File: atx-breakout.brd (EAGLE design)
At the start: 160 x 100 mm, 103 parts, among them J1 61400826021, J10 CON_TERMINAL_BLOCK_02-5MM, J11 61400826021, J2 61400826021, J3 Molex KK 47053-1000, J4 Molex KK 47053-1000, J5 Molex KK 47053-1000, J6 Molex KK 47053-1000, J7 61400826021, J8 CON_TERMINAL_BLOCK_02-5MM, J9 CON_TERMINAL_BLOCK_02-5MM, Q1 IRF9530, Q2 IRF9530, Q3 IRF9530, Q4 IRF9530, Q5 IRF9530, Q6 IRF9530, Q7 IRF9530, T1 2N3904, T2 2N3904, T3 2N3904, T4 2N3904, T5 2N3904, T6 2N3904, T7 2N3904, X10 MA02-1JC, X12 XT30-J, X13 MA02-1JC, X15 XT30-J, X16 MA02-1JC, X17 CONN-IDC-10PS, X18 CONN-IDC-10PS, X2 XT30-J, X20 XT30-J, X21 MA02-1JC, X3 MA02-1JC, X4 XT30-J, X5 MA02-1JC, X6 XT30-J, X7 MA02-1JC, X9 XT30-J

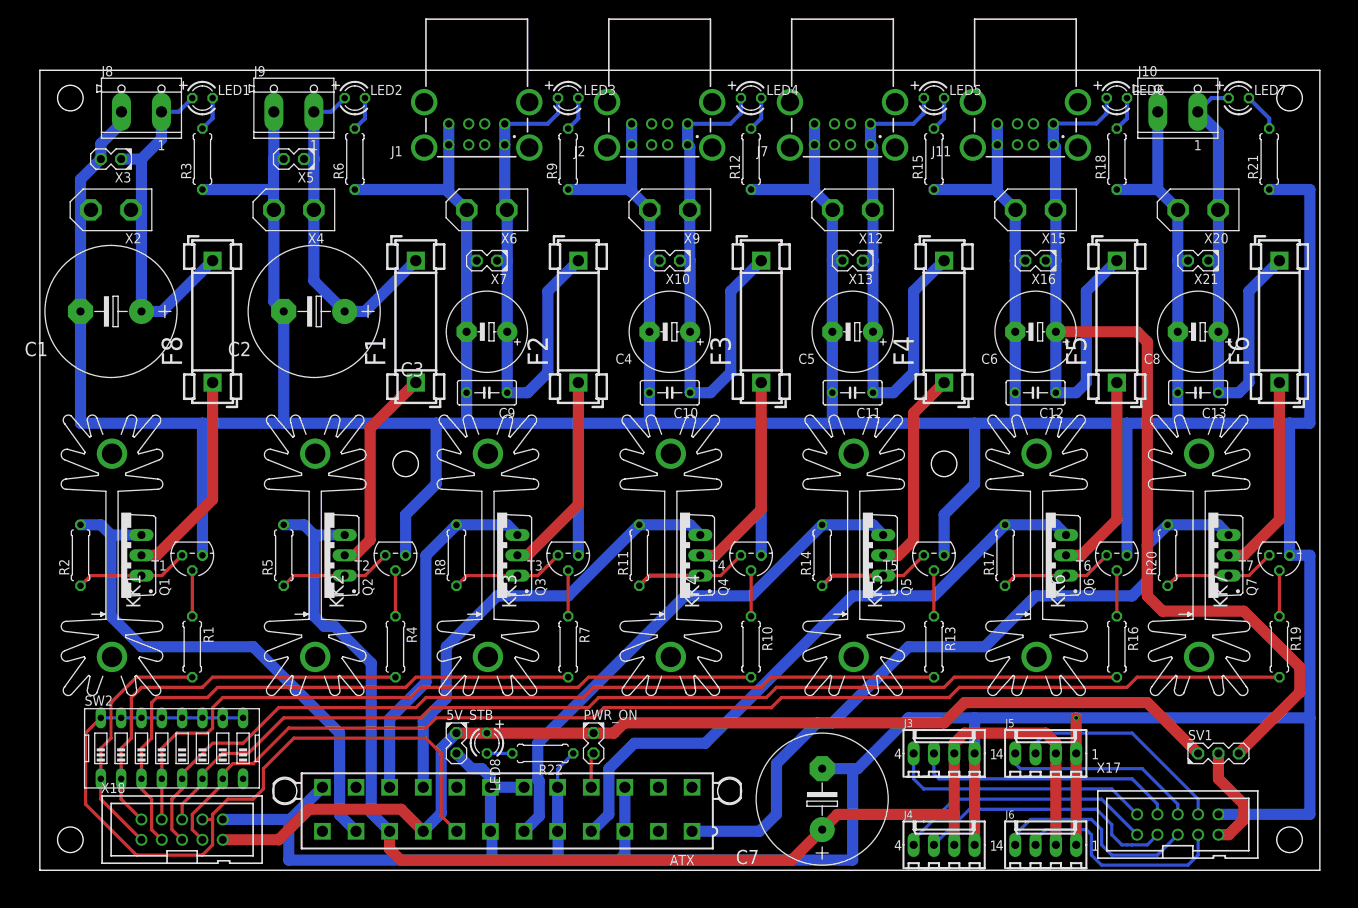
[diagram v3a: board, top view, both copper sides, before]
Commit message: Separate grounds for every channel
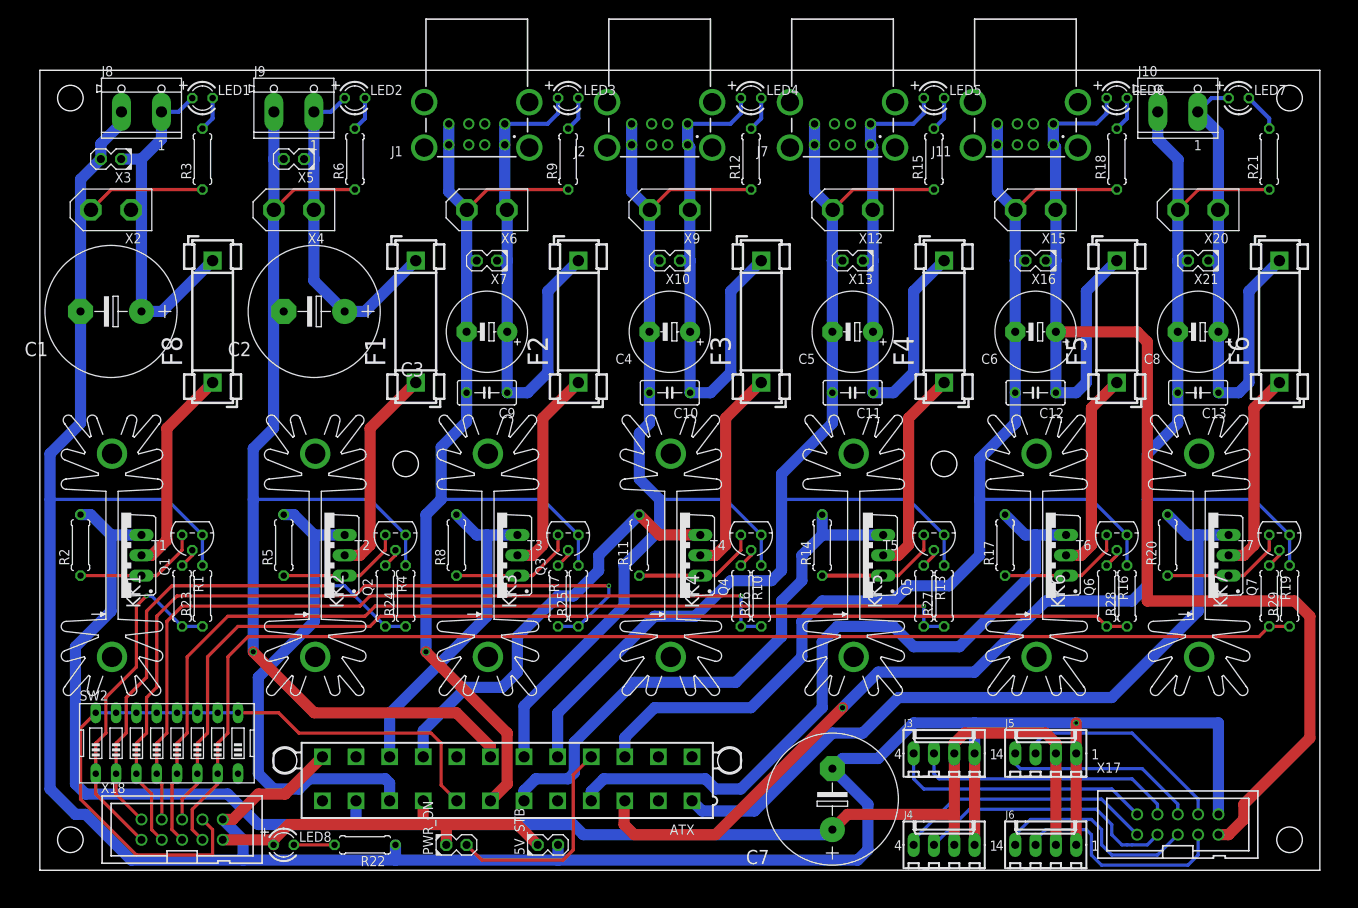
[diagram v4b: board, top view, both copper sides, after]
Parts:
- removed SV1: (no value), joakim:MA03-1J
- added R23, R24, R25, R26, R27, R28, R29: 1k, rcl:0207/7
- moved LED8 28.4 mm to (30.5, 3.17), turned to 0 degrees
- moved R22 25.0 mm to (40.6, 3.17)
- moved PWR_ON 19.6 mm to (53.3, 3.17), turned to 0 degrees
- moved 5V_STB 17.1 mm to (64.8, 3.17), turned to 0 degrees
- moved R10 6.48 mm to (87.6, 34.3)
- moved R13 6.48 mm to (110.5, 34.3)
- moved R16 6.48 mm to (133.3, 34.3)
- moved R19 6.48 mm to (153.7, 34.3)
- moved R7 6.48 mm to (64.8, 34.3)
- moved R1 6.48 mm to (17.8, 34.3)
- moved R4 6.48 mm to (43.2, 34.3)
- moved ATX 3.81 mm to (58.4, 11.4)
- moved T1 2.54 mm to (19.1, 41.9)
- moved T2 2.54 mm to (44.5, 41.9)
- moved T3 2.54 mm to (66.0, 41.9)
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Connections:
- removed net N$32: SV1.2, X17.9
- new net GND1: ATX.19, C2.-, J9.2, R24.2, R6.1, T2.3, X4.1, X5.2
- new net GND2: ATX.7, C3.-, C9.2, J1.4, J1.8, R25.2, R9.1, T3.3, X6.1, X7.2
- new net GND3: ATX.18, C10.2, C4.-, J2.4, J2.8, R12.1, R26.2, T4.3, X10.2, X9.1
- new net GND4: ATX.17, C11.2, C5.-, J7.4, J7.8, R15.1, R27.2, T5.3, X12.1, X13.2
- new net GND5: ATX.15, C12.2, C6.-, J11.4, J11.8, R18.1, R28.2, T6.3, X15.1, X16.2
- new net GNDA: ATX.3, C13.2, C8.-, J10.2, R21.1, R29.2, T7.3, X20.1, X21.2
- net +12V/1: no longer C7.+, J3.2, J4.2, J5.2, J6.2
- net +12V/2: now also C7.+, J3.2, J4.2, J5.2, J6.2
- net +5V_STB: no longer SV1.1
- net GND: now also R23.2; no longer ATX.15, ATX.17, ATX.18, ATX.19, ATX.3, ATX.5, ATX.7, C10.2, C11.2, C12.2, C13.2, C2.-, C3.-, C4.-, C5.-, C6.-, C8.-, C9.2, J1.4, J1.8, J10.2, J11.4, J11.8, J2.4, J2.8, J7.4, J7.8, J9.2, R12.1, R15.1, R18.1, R21.1, R6.1, R9.1, T2.3, T3.3, T4.3, T5.3, T6.3, T7.3, X10.2, X12.1, X13.2, X15.1, X16.2, X20.1, X21.2, X4.1, X5.2, X6.1, X7.2, X9.1
- net PWR_CTRL_12V1: now also R23.1
- net PWR_CTRL_12V2: now also R24.1
- net PWR_CTRL_3V1: now also R29.1
- net PWR_CTRL_5V1: now also R25.1
- net PWR_CTRL_5V2: now also R26.1
- net PWR_CTRL_5V3: now also R27.1
- net PWR_CTRL_5V4: now also R28.1
- net SW5V1: now also X17.9; no longer SV1.3
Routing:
- net GND: track 926.2 -> 366.0 mm
- net GNDA: track 0.00 -> 180.9 mm, vias 0 -> 1
- net GND5: track 0.00 -> 154.6 mm
- net GND1: track 0.00 -> 142.8 mm, vias 0 -> 1
- net GND4: track 0.00 -> 141.2 mm
- net +12V/2: track 66.1 -> 197.3 mm
- net GND2: track 0.00 -> 130.5 mm, vias 0 -> 1
- net GND3: track 0.00 -> 122.0 mm
- net +12V/1: track 164.7 -> 61.6 mm
- net +5V_STB: track 138.7 -> 47.5 mm
- net PWR_CTRL_5V1: track 72.1 -> 97.6 mm, vias 0 -> 1
- net PWR_ON: track 4.36 -> 27.2 mm
- net SW5V1: track 145.7 -> 163.5 mm
- net PWR_CTRL_5V2: track 87.7 -> 105.0 mm, vias 0 -> 1
- net PWR_CTRL_5V3: track 108.3 -> 124.0 mm, vias 0 -> 1
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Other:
- board text removed: "Separate GNDs per lane?"
- board text removed: "Should 10 and 11 be routed down and around instead?"

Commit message: More mounting holes, screw terminal for 10Ohm load
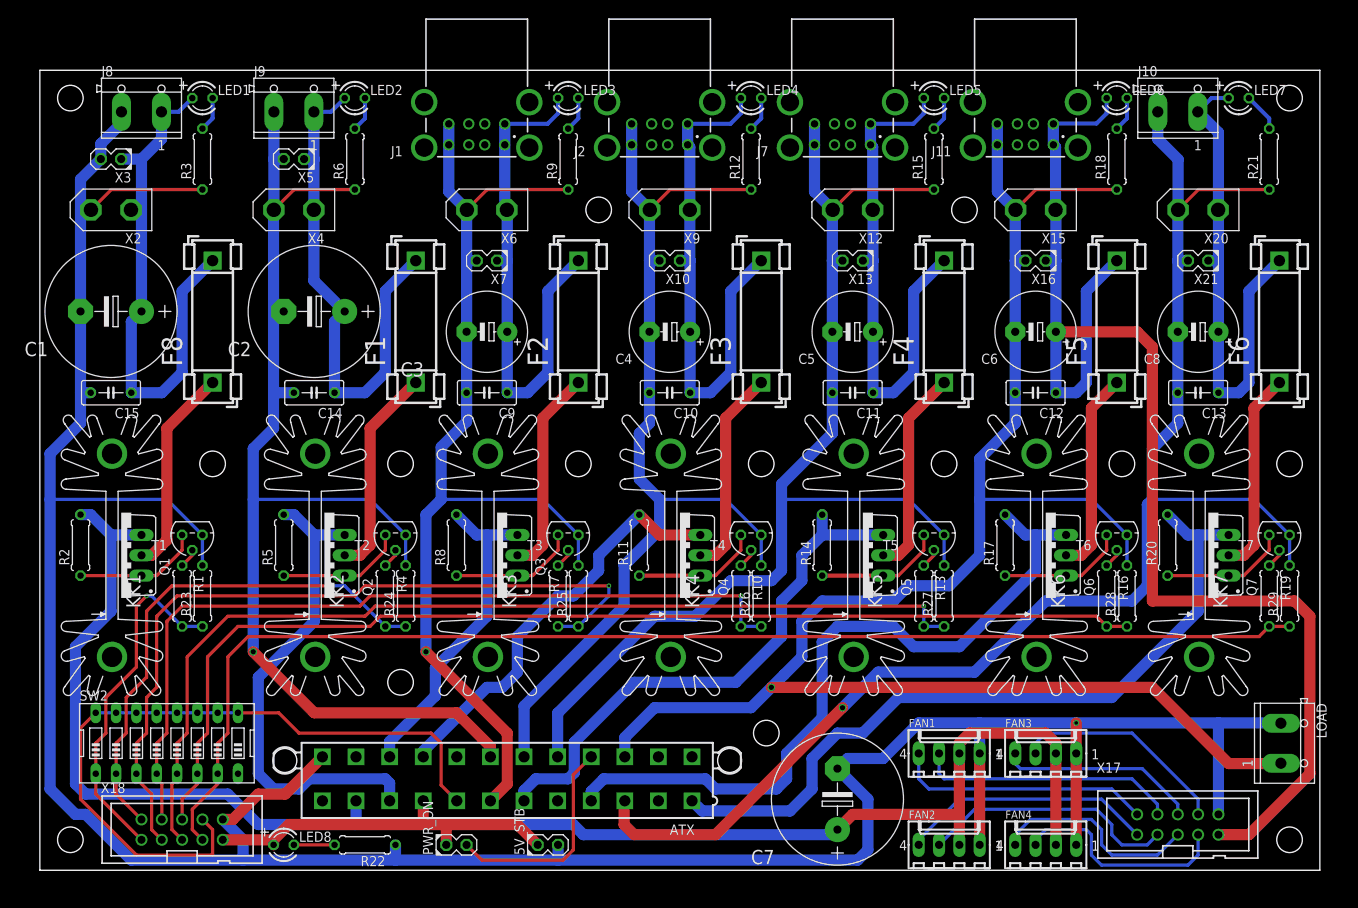
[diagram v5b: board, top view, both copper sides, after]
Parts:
- removed J3, J4: Molex KK 47053-1000, con-molex:6410-04
- added C14, C15: (no value), rcl:C050-030X075
- added FAN1, FAN2: Molex KK 47053-1000, con-molex:6410-04
- added LOAD: CON_TERMINAL_BLOCK_02-5MM, dp_devices.v6:TERMINAL_BLOCK_2P_5
- moved C7 0.63 mm to (99.7, 8.89)
- renumbered J5 to FAN3, J6 to FAN4
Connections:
- net +12V/2: now also FAN1.2, FAN2.2; no longer J3.2, J4.2
- net FAN1_CTRL: now also FAN1.4; no longer J3.4
- net FAN1_SENSE: now also FAN1.3; no longer J3.3
- net FAN2_CTRL: now also FAN2.4; no longer J4.4
- net FAN2_SENSE: now also FAN2.3; no longer J4.3
- net GND: now also C15.2, FAN1.1, FAN2.1, LOAD.2; no longer J3.1, J4.1
- net GND1: now also C14.2
- net GND5: now also LOAD.1
- net N$4: now also C15.1
- net N$9: now also C14.1
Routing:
- net GND5: track 154.6 -> 222.2 mm, vias 0 -> 1
- net N$9: track 44.0 -> 66.1 mm
- net N$4: track 45.9 -> 68.0 mm
- net GND: track 366.0 -> 374.2 mm
- net +5V/1: track 89.3 -> 91.9 mm
- net GND1: track 142.8 -> 145.3 mm
- net +3V3/1: track 92.3 -> 94.6 mm
- net +5V/3: track 53.8 -> 52.4 mm
- net SW5V1: track 163.5 -> 164.6 mm
- net FAN2_CTRL: track 32.5 -> 31.9 mm
- net FAN1_CTRL: track 33.0 -> 32.3 mm
- net FAN1_SENSE: track 33.3 -> 32.7 mm
- net FAN2_SENSE: track 32.9 -> 32.3 mm
- net GNDA: track 180.9 -> 180.2 mm

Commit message: Updated XT-30 footprint, updated pulldown resistor value
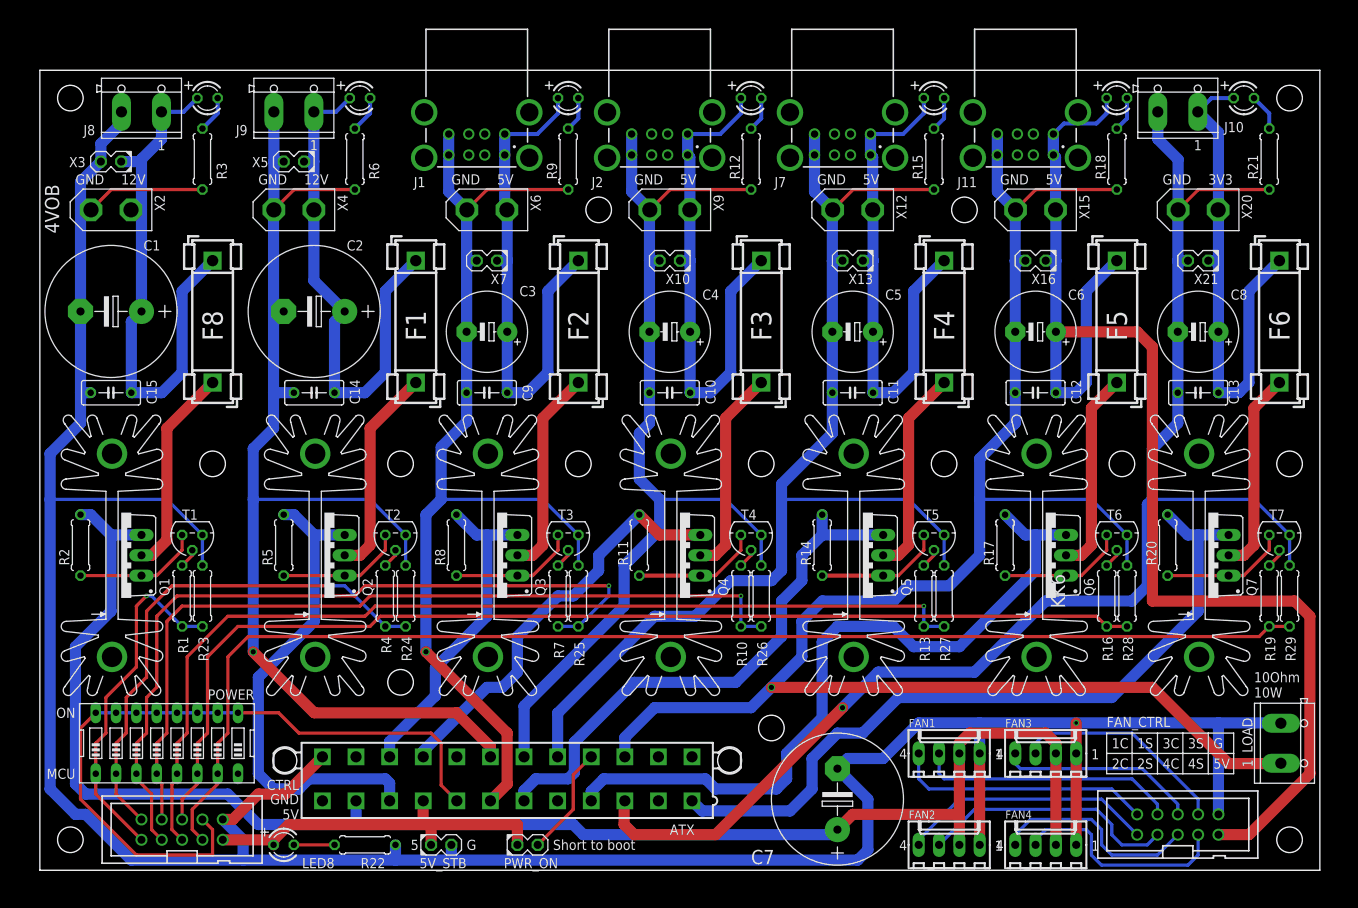
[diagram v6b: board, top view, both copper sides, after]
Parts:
- added U$1: (no value), joakim:XONIK_LOGO_60
- R23, R24, R25, R26, R27, R28, R29: value 1k -> 10k
- moved 5V_STB 13.3 mm to (51.4, 3.17)
- moved PWR_ON 8.89 mm to (62.2, 3.17)
- moved J1 1.27 mm to (54.6, 96.5)
- moved J11 1.27 mm to (123.2, 96.5)
- moved J2 1.27 mm to (77.5, 96.5)
- moved J7 1.27 mm to (100.3, 96.5)
- moved LED2 0.64 mm to (40.0, 96.5)
- moved LED1 0.63 mm to (21.0, 96.5)
- moved LED7 0.63 mm to (150.5, 96.5)
- moved X3 0.32 mm to (7.62, 88.6)
- moved X5 0.32 mm to (30.5, 88.6)
- renumbered SW2 to POWER, X17 to FAN_CTRL, X18 to CTRL
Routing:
- net PWR_ON: track 27.2 -> 13.8 mm
- net N$9: track 66.1 -> 67.7 mm
- net GND5: track 222.2 -> 221.0 mm
- net GND3: track 122.0 -> 120.7 mm
- net GND4: track 141.2 -> 139.9 mm
- net GND2: track 130.5 -> 129.3 mm
- net +5V_STB: track 47.5 -> 46.4 mm
- net N$24: track 65.8 -> 65.1 mm
- net N$19: track 65.8 -> 65.1 mm
- net N$14: track 65.8 -> 65.1 mm
- net SW5V1: track 164.6 -> 163.9 mm
- net N$4: track 68.0 -> 68.7 mm
- net N$35: track 63.2 -> 63.9 mm
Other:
- board text added: "10Ohm 10W"
- board text added: "12V"
- board text added: "1C"
- board text added: "1S"
- board text added: "2C"
- board text added: "2S"
- board text added: "3C"
- board text added: "3S"
- board text added: "3V3"
- board text added: "4C"
- board text added: "4S"
- board text added: "4VOB"
- board text added: "5"
- board text added: "5V"
- board text added: "ATX PSU Breakout board"
- board text added: "G"
- board text added: "GND"
- board text added: "MCU"
- board text added: "ON"
- board text added: "Short to boot"
- board text added: "v1.0"
